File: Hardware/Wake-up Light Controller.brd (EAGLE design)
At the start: 85.7 x 54 mm, 47 parts, among them IC1 ST1S10, IC2 HT7333, IC3 DS3231/SO, IC4 ATMEGA328P_TQFP, J1 AVR-ISP, J2 Debug, Q1 BSS138, Q2 BSS138, Q3 FDN306P, Q4 IRLZ44N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

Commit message: Move via
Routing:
- net +5V: track 157.0 -> 159.2 mm
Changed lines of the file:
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@@
 <wire x1="5.715" y1="40.64" x2="7.305" y2="40.64" width="0.4064" layer="1"/>
 <wire x1="7.305" y1="40.64" x2="7.305" y2="43.18" width="0.4064" layer="1"/>
-<wire x1="35.56" y1="16.03" x2="35.56" y2="15.875" width="0.4064" layer="1"/>
-<wire x1="35.56" y1="15.875" x2="34.29" y2="14.605" width="0.4064" layer="1"/>
+<wire x1="35.56" y1="16.03" x2="35.56" y2="13.97" width="0.4064" layer="1"/>
+<wire x1="35.56" y1="13.97" x2="34.29" y2="12.7" width="0.4064" layer="1"/>
+<wire x1="34.29" y1="12.7" x2="30.265" y2="12.7" width="0.4064" layer="1"/>
 <wire x1="35.56" y1="16.03" x2="36.35" y2="16.03" width="0.4064" layer="1"/>
 <wire x1="36.35" y1="16.03" x2="37.465" y2="17.145" width="0.4064" layer="1"/>
@@
 <wire x1="34.6075" y1="29.21" x2="34.6075" y2="27.6225" width="0.4064" layer="1"/>
 <wire x1="34.6075" y1="27.6225" x2="37.465" y2="24.765" width="0.4064" layer="1"/>
-<wire x1="30.265" y1="13.12" x2="29.845" y2="12.7" width="0.4064" layer="1"/>
-<wire x1="30.265" y1="14.605" x2="30.265" y2="21.59" width="0.4064" layer="1"/>
-<wire x1="30.265" y1="14.605" x2="30.265" y2="13.12" width="0.4064" layer="1"/>
-<wire x1="34.29" y1="14.605" x2="30.265" y2="14.605" width="0.4064" layer="1"/>
+<wire x1="30.265" y1="12.7" x2="30.265" y2="21.59" width="0.4064" layer="1"/>
 <wire x1="36.195" y1="41.717" x2="33.782" y2="41.717" width="0.4064" layer="1"/>
 <wire x1="33.782" y1="41.717" x2="33.655" y2="41.59" width="0.4064" layer="1"/>
@@
 <wire x1="33.34" y1="42.86" x2="33.655" y2="42.545" width="0.4064" layer="1"/>
 <wire x1="33.655" y1="42.545" x2="33.655" y2="41.59" width="0.4064" layer="1"/>
+<wire x1="29.845" y1="12.7" x2="30.265" y2="12.7" width="0.4064" layer="1"/>
 </signal>
 <signal name="N$7">
@@
 <contactref element="POTENTIOMETER" pad="2"/>
 <wire x1="24.225" y1="31.655" x2="24.225" y2="31.9024" width="0.4064" layer="1"/>
-<wire x1="33.02" y1="5.695" x2="33.02" y2="16.51" width="0.4064" layer="16"/>
-<via x="33.02" y="16.51" extent="1-16" drill="0.8" diameter="1.778"/>
-<wire x1="33.655" y1="17.145" x2="33.02" y2="16.51" width="0.4064" layer="1"/>
-<wire x1="33.655" y1="24.13" x2="33.655" y2="17.145" width="0.4064" layer="1"/>
+<wire x1="33.02" y1="5.695" x2="33.02" y2="14.605" width="0.4064" layer="16"/>
+<via x="33.02" y="14.605" extent="1-16" drill="0.8" diameter="1.778"/>
+<wire x1="33.655" y1="15.24" x2="33.02" y2="14.605" width="0.4064" layer="1"/>
+<wire x1="33.655" y1="24.13" x2="33.655" y2="15.24" width="0.4064" layer="1"/>
 <wire x1="24.225" y1="31.9024" x2="24.225" y2="29.75" width="0.4064" layer="1"/>
 <wire x1="24.225" y1="29.75" x2="25.4" y2="28.575" width="0.4064" layer="1"/>

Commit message: Changed battery holder name
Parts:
- renumbered U$1 to J3
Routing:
- net N$9: track 66.4 -> 67.3 mm
- net +5V: track 159.2 -> 158.6 mm
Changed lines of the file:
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@@
 <attribute name="VALUE" x="50.165" y="40.9575" size="1" layer="27"/>
 </element>
-<element name="U$1" library="heol" package="BATTCON_16MM_PTH" value="CR1632_3V" x="78.74" y="31.75" smashed="yes" rot="R270">
+<element name="J3" library="heol" package="BATTCON_16MM_PTH" value="CR1632_3V" x="78.74" y="31.75" smashed="yes" rot="R270">
 <attribute name="NAME" x="75.438" y="31.845" size="1" layer="25" font="vector" ratio="11" rot="R90" align="bottom-center"/>
 <attribute name="VALUE" x="80.772" y="18.51" size="1" layer="27" font="vector" ratio="11" rot="R90" align="top-center"/>
@@
 <wire x1="22.625" y1="29.295" x2="22.625" y2="31.9024" width="0.4064" layer="1"/>
 <wire x1="22.625" y1="29.295" x2="22.54" y2="29.21" width="0.4064" layer="1"/>
-<contactref element="U$1" pad="GND"/>
+<contactref element="J3" pad="GND"/>
 <wire x1="55.245" y1="23.91" x2="68.245" y2="23.91" width="0.4064" layer="1"/>
 <wire x1="24.13" y1="45.72" x2="23.495" y2="46.355" width="0.4064" layer="1"/>
@@
 <contactref element="L1" pad="2"/>
 <contactref element="R3" pad="1"/>
-<wire x1="29.845" y1="21.17" x2="30.265" y2="21.59" width="0.8128" layer="1"/>
-<wire x1="30.265" y1="22.44" x2="30.265" y2="21.59" width="0.8128" layer="1"/>
 <via x="29.845" y="12.7" extent="1-16" drill="0.8" diameter="1.778"/>
 <wire x1="36.96" y1="45.87875" x2="34.66" y2="45.87875" width="0.8128" layer="1"/>
@@
 <contactref element="R6" pad="1"/>
 <contactref element="R8" pad="1"/>
-<wire x1="30.265" y1="21.59" x2="30.265" y2="21.375" width="0.4064" layer="1"/>
 <contactref element="R1" pad="1"/>
 <contactref element="R2" pad="1"/>
@@
 <wire x1="21.825" y1="31.9024" x2="21.825" y2="36.83" width="0.4064" layer="1"/>
 <wire x1="21.825" y1="36.83" x2="21.825" y2="38.335" width="0.4064" layer="1"/>
-<wire x1="30.265" y1="21.59" x2="30.265" y2="23.71" width="0.8128" layer="1"/>
-<wire x1="30.265" y1="23.71" x2="26.67" y2="27.305" width="0.8128" layer="1"/>
-<wire x1="20.32" y1="27.305" x2="26.67" y2="27.305" width="0.8128" layer="1"/>
-<wire x1="20.32" y1="27.305" x2="16.024" y2="27.305" width="0.8128" layer="1"/>
+<wire x1="20.32" y1="27.305" x2="28.575" y2="27.305" width="0.8128" layer="1"/>
+<wire x1="28.575" y1="27.305" x2="30.265" y2="25.615" width="0.8128" layer="1"/>
+<wire x1="30.265" y1="25.615" x2="30.265" y2="21.59" width="0.8128" layer="1"/>
+<wire x1="16.024" y1="27.305" x2="20.32" y2="27.305" width="0.8128" layer="1"/>
 <wire x1="16.024" y1="27.305" x2="15.77" y2="27.559" width="0.8128" layer="1"/>
 <wire x1="20.64" y1="29.21" x2="20.64" y2="27.625" width="0.4064" layer="1"/>
@@
 <contactref element="IC3" pad="14"/>
 <contactref element="C7" pad="2"/>
-<contactref element="U$1" pad="VCC@2" route="any" routetag="G$1.VCC"/>
-<contactref element="U$1" pad="VCC@1" route="any" routetag="G$1.VCC"/>
+<contactref element="J3" pad="VCC@2" route="any" routetag="G$1.VCC"/>
+<contactref element="J3" pad="VCC@1" route="any" routetag="G$1.VCC"/>
 <wire x1="78.74" y1="23.146" x2="78.74" y2="22.86" width="0.4064" layer="1"/>
 <wire x1="78.74" y1="22.86" x2="76.2" y2="20.32" width="0.4064" layer="1"/>
@@
 <wire x1="9.161" y1="20.32" x2="8.255" y2="20.32" width="0.8128" layer="1"/>
 <wire x1="9.161" y1="20.32" x2="9.161" y2="21.59" width="0.8128" layer="1"/>
-<wire x1="17.78" y1="17.145" x2="15.875" y2="19.05" width="0.8128" layer="1"/>
+<wire x1="18.415" y1="16.51" x2="15.875" y2="19.05" width="0.8128" layer="1"/>
 <wire x1="15.875" y1="19.05" x2="14.969" y2="19.05" width="0.8128" layer="1"/>
 <contactref element="F1" pad="P$2"/>
@@
 <via x="15.5575" y="23.8125" extent="1-16" drill="0.8" diameter="1.778"/>
 <wire x1="15.5575" y1="23.8125" x2="15.5575" y2="23.97125" width="0.8128" layer="1"/>
-<wire x1="15.5575" y1="23.97125" x2="16.8275" y2="25.24125" width="0.8128" layer="1"/>
-<wire x1="16.8275" y1="25.24125" x2="23.01875" y2="25.24125" width="0.8128" layer="1"/>
+<wire x1="15.5575" y1="23.97125" x2="17.4625" y2="25.87625" width="0.8128" layer="1"/>
+<wire x1="24.765" y1="16.51" x2="24.765" y2="25.87625" width="0.8128" layer="1"/>
+<wire x1="24.765" y1="25.87625" x2="17.4625" y2="25.87625" width="0.8128" layer="1"/>
 <wire x1="6.985" y1="21.59" x2="9.161" y2="21.59" width="0.8128" layer="1"/>
 <wire x1="20.32" y1="13.65" x2="18.415" y2="13.65" width="0.8128" layer="1"/>
 <wire x1="20.32" y1="13.65" x2="20.574" y2="13.65" width="0.8128" layer="1"/>
-<wire x1="20.32" y1="17.145" x2="17.78" y2="17.145" width="0.8128" layer="1"/>
-<wire x1="20.32" y1="17.145" x2="20.32" y2="13.65" width="0.8128" layer="1"/>
+<wire x1="20.32" y1="16.51" x2="18.415" y2="16.51" width="0.8128" layer="1"/>
+<wire x1="20.32" y1="16.51" x2="20.32" y2="13.65" width="0.8128" layer="1"/>
 <contactref element="D1" pad="C"/>
-<wire x1="23.01875" y1="25.24125" x2="25.4" y2="22.86" width="0.8128" layer="1"/>
-<wire x1="25.4" y1="17.145" x2="25.4" y2="22.86" width="0.8128" layer="1"/>
-<wire x1="25.4" y1="17.145" x2="25.4" y2="13.765" width="0.8128" layer="1"/>
-<wire x1="25.4" y1="13.765" x2="26.465" y2="12.7" width="0.8128" layer="1"/>
-<wire x1="20.32" y1="17.145" x2="25.4" y2="17.145" width="0.8128" layer="1"/>
+<wire x1="24.765" y1="16.51" x2="24.765" y2="14.4" width="0.8128" layer="1"/>
+<wire x1="24.765" y1="14.4" x2="26.465" y2="12.7" width="0.8128" layer="1"/>
+<wire x1="20.32" y1="16.51" x2="24.765" y2="16.51" width="0.8128" layer="1"/>
 <wire x1="10.795" y1="25.4" x2="7.62" y2="28.575" width="0.8128" layer="16"/>
 <wire x1="7.62" y1="28.575" x2="7.62" y2="29.845" width="0.8128" layer="16"/>

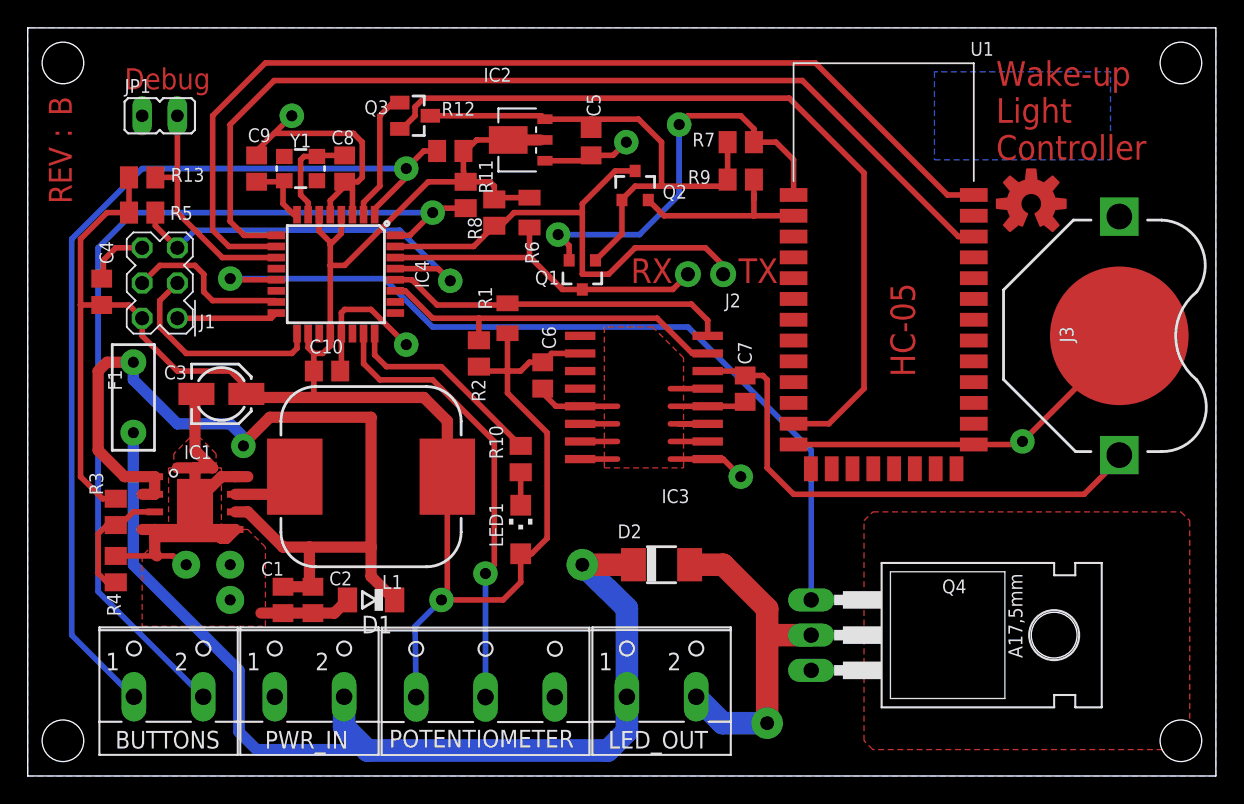
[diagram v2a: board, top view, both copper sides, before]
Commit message: Changed inductor package
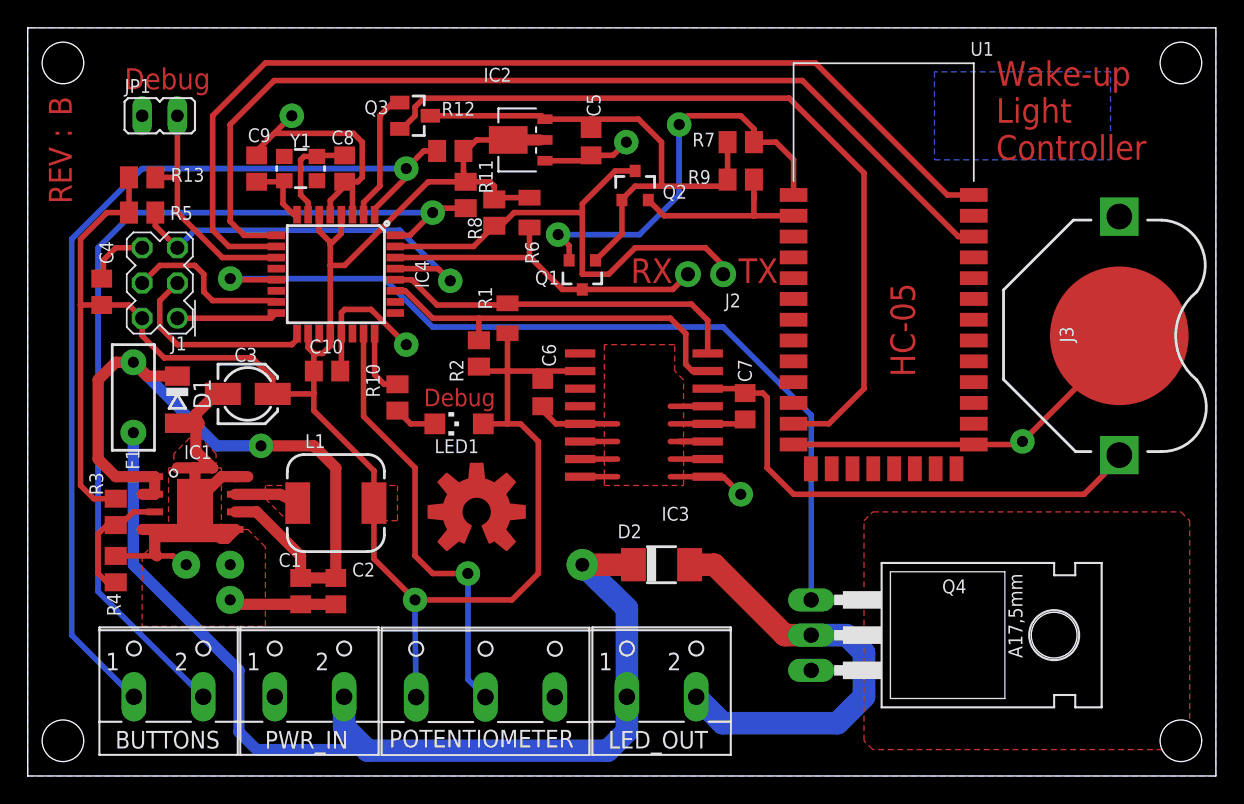
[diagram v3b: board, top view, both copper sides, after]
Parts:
- L1: device inductor-sumida:CDRH127/LD -> inductor-wurth:74437346068
- LOGO1: value OSHW-LOGOM-COPPER -> OSHW-LOGOL-COPPER; device SparkFun-Aesthetics:OSHW-LOGO-M_COPPER -> SparkFun-Aesthetics:OSHW-LOGO-L_COPPER
- moved LOGO1 45.8 mm to (32.4, 19.1)
- moved D1 20.1 mm to (10.8, 27.1), turned to 270 degrees
- moved R10 9.94 mm to (26.7, 27.3)
- moved LED1 8.82 mm to (31.1, 25.4), turned to 90 degrees
- moved L1 3.18 mm to (22.2, 19.7)
- moved C3 1.90 mm to (15.9, 27.6)
- moved C2 1.77 mm to (22.2, 13.3)
- moved C1 1.42 mm to (19.7, 13.3)
- moved C6 1.27 mm to (37.1, 27.6)
- moved C7 1.27 mm to (51.8, 26.7)
- moved IC3 1.27 mm to (44.5, 26.0)
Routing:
- net N$9: track 67.3 -> 55.0 mm
- net N$3: track 14.8 -> 4.89 mm
- net N$1: track 24.2 -> 32.1 mm, vias 1 -> 0
- net GND: track 145.1 -> 148.7 mm
- net +5V: track 158.6 -> 156.6 mm
- net SDA: track 26.0 -> 27.8 mm
- net VBAT: track 38.7 -> 37.0 mm
- net N$10: track 61.2 -> 62.7 mm
- net N$8: track 2.38 -> 3.76 mm
- net N$11: track 32.9 -> 31.6 mm
- net SCK: track 15.6 -> 14.7 mm
- net SCL: track 25.4 -> 26.3 mm
- added copper zone on layer 1, net +5V
- added copper zone on layer 1, net N$6

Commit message: Modify copper traces
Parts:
- moved JP1 1.27 mm to (9.53, 46.4)
- moved D2 0.63 mm to (45.1, 15.2)
- moved R10 0.63 mm to (27.3, 27.3)
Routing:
- net +5V: track 156.6 -> 160.9 mm
- net GND: track 148.7 -> 146.4 mm
- net DEBUG: track 17.1 -> 15.8 mm
- net N$8: track 3.76 -> 3.13 mm
- net N$3: track 4.89 -> 5.52 mm
- net N$1: track 32.1 -> 32.7 mm
- net +12V: track 75.5 -> 74.9 mm
- net RST: track 29.2 -> 28.7 mm

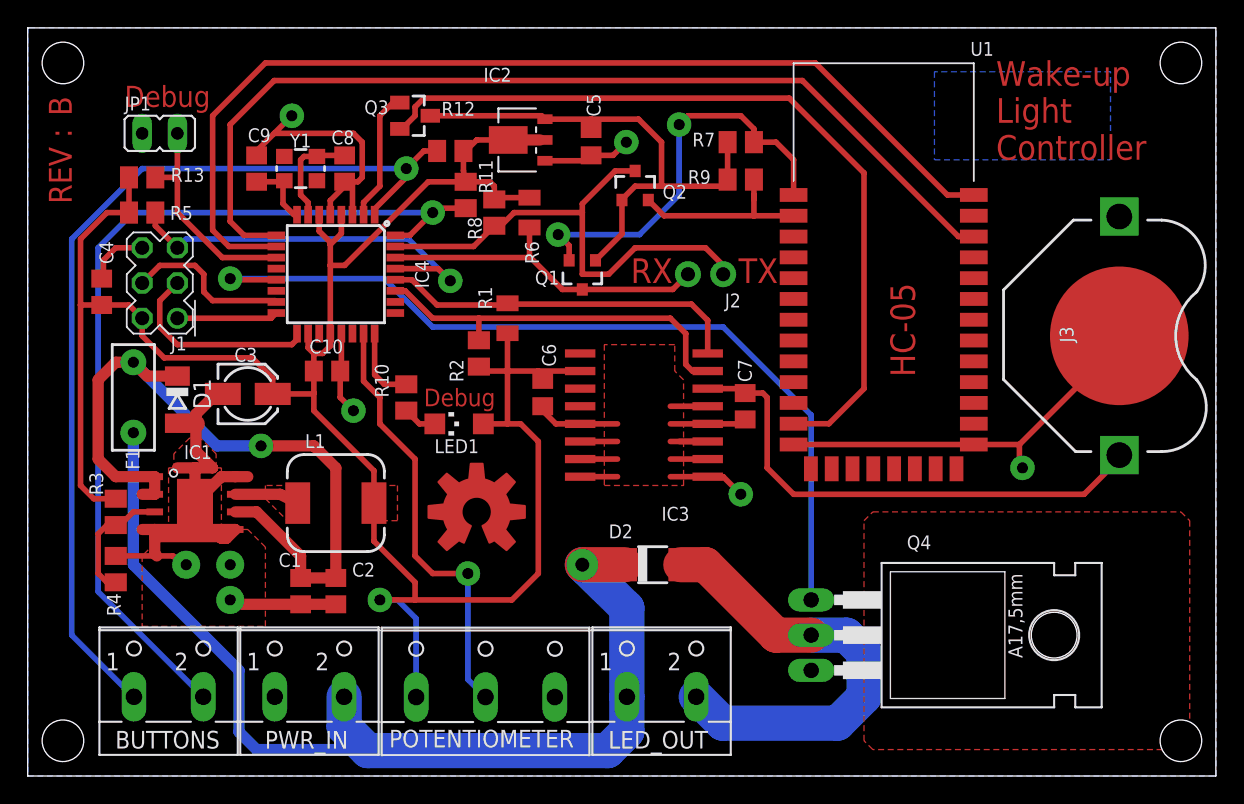
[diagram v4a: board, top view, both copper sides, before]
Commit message: Isolate ADC trace from switching PSU
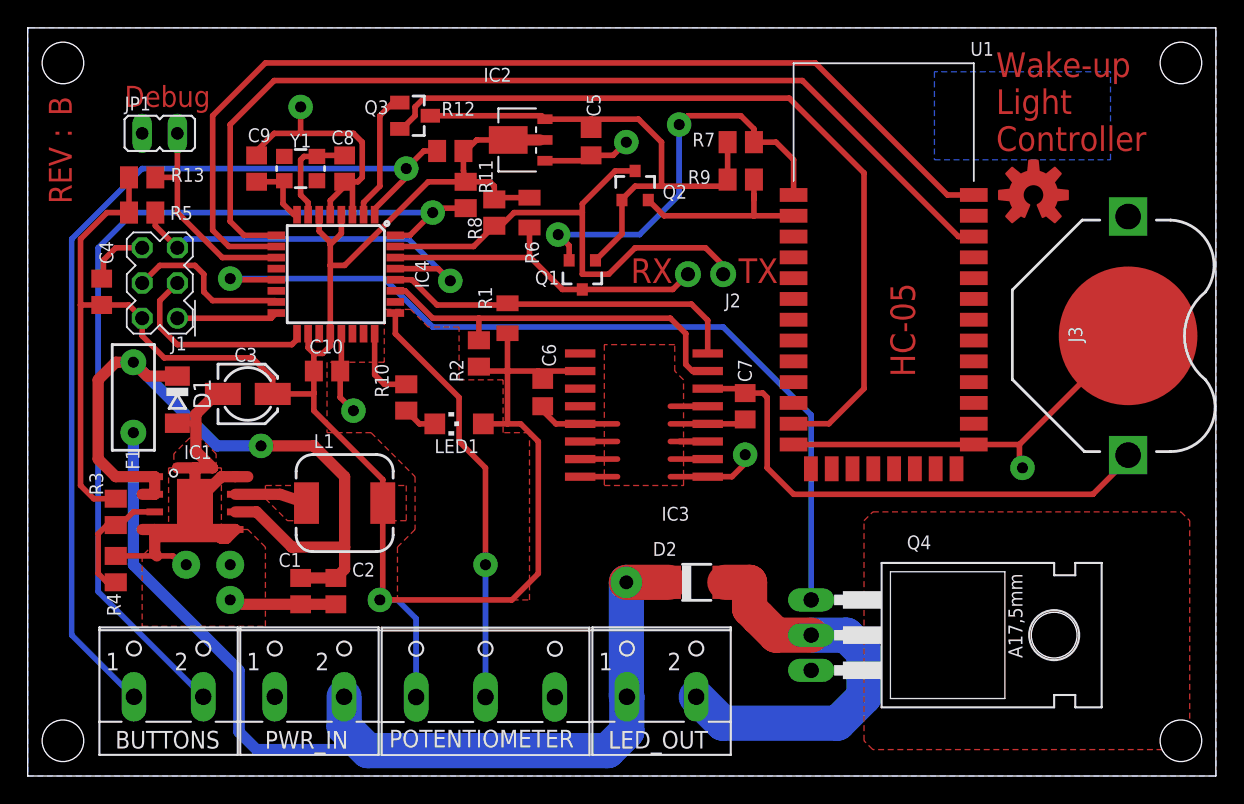
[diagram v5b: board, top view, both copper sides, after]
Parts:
- LOGO1: value OSHW-LOGOL-COPPER -> OSHW-LOGOM-COPPER; device SparkFun-Aesthetics:OSHW-LOGO-L_COPPER -> SparkFun-Aesthetics:OSHW-LOGO-M_COPPER
- moved LOGO1 46.2 mm to (72.5, 41.9)
- moved D2 3.42 mm to (48.3, 14.0)
- moved J3 0.64 mm to (79.4, 31.8)
- moved L1 0.63 mm to (22.9, 19.7)
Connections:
- net N$11: now also IC4.25; no longer IC4.23
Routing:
- net +12V: track 74.9 -> 72.3 mm
- net N$1: track 32.7 -> 30.1 mm
- net N$9: track 55.0 -> 56.9 mm
- net GND: track 146.4 -> 147.6 mm
- net N$11: track 31.6 -> 30.4 mm
- net +5V: track 160.9 -> 160.1 mm
- net VBAT: track 37.0 -> 37.7 mm
- net N$6: track 4.66 -> 5.24 mm

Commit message: Optimize layout
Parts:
- moved R8 5.17 mm to (38.6, 42.2), turned to 0 degrees
- moved R6 4.07 mm to (33.7, 37.5)
- moved R11 1.99 mm to (33.3, 41.0), turned to 180 degrees
- moved R1 1.27 mm to (35.9, 33.0)
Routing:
- net +5V: track 160.1 -> 164.8 mm
- net BT_TX: track 30.1 -> 32.4 mm
- net MCU_RX: track 24.7 -> 22.5 mm
- net N$7: track 9.13 -> 10.4 mm
- net MCU_TX: track 36.5 -> 37.7 mm
- net SCL: track 26.3 -> 27.2 mm
- net ALRM_BTN: track 66.6 -> 67.4 mm
